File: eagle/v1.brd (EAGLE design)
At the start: 24.2 x 49.6 mm, 48 parts, among them IC2 LT1761, IC4 LT1376-ADJ, Q1 12Mhz, T1 Si2301DS, X1 USB-MICROB

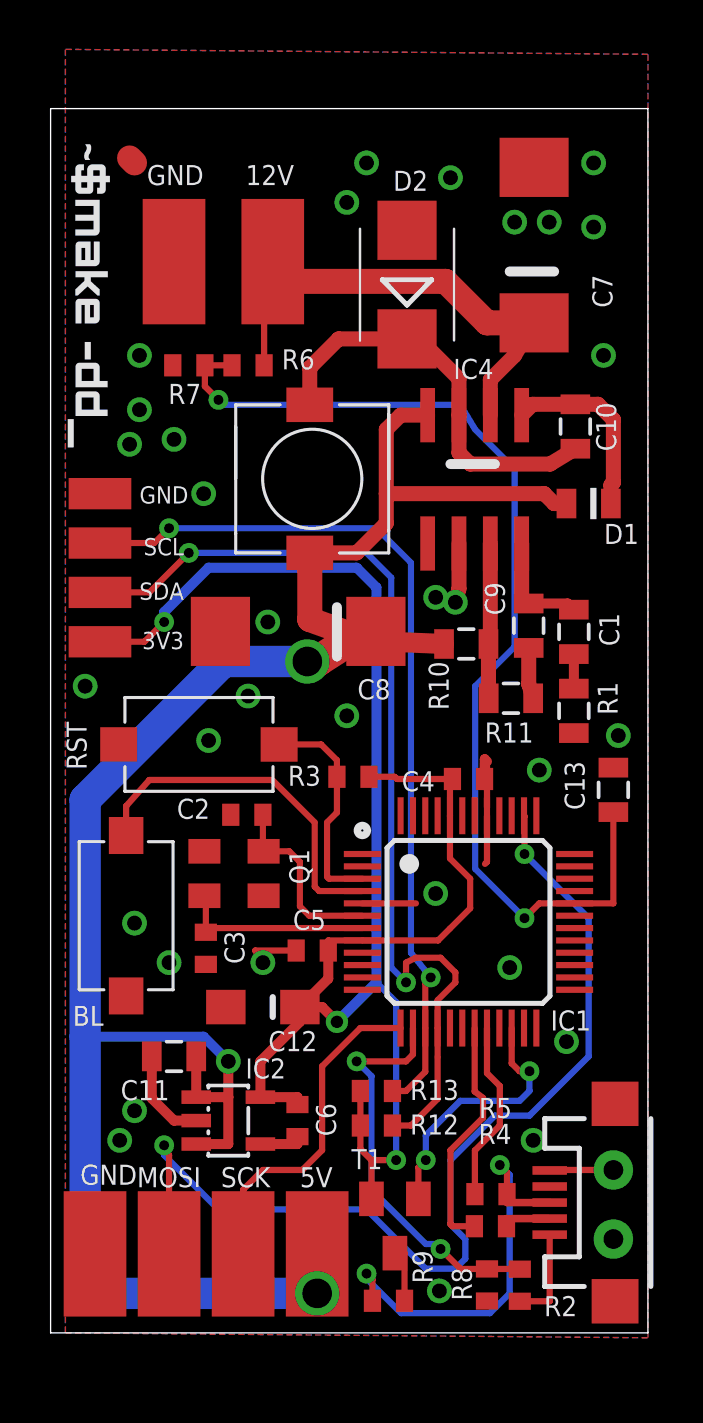
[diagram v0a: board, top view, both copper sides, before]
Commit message: supply circuit via USB for firmware upgrades
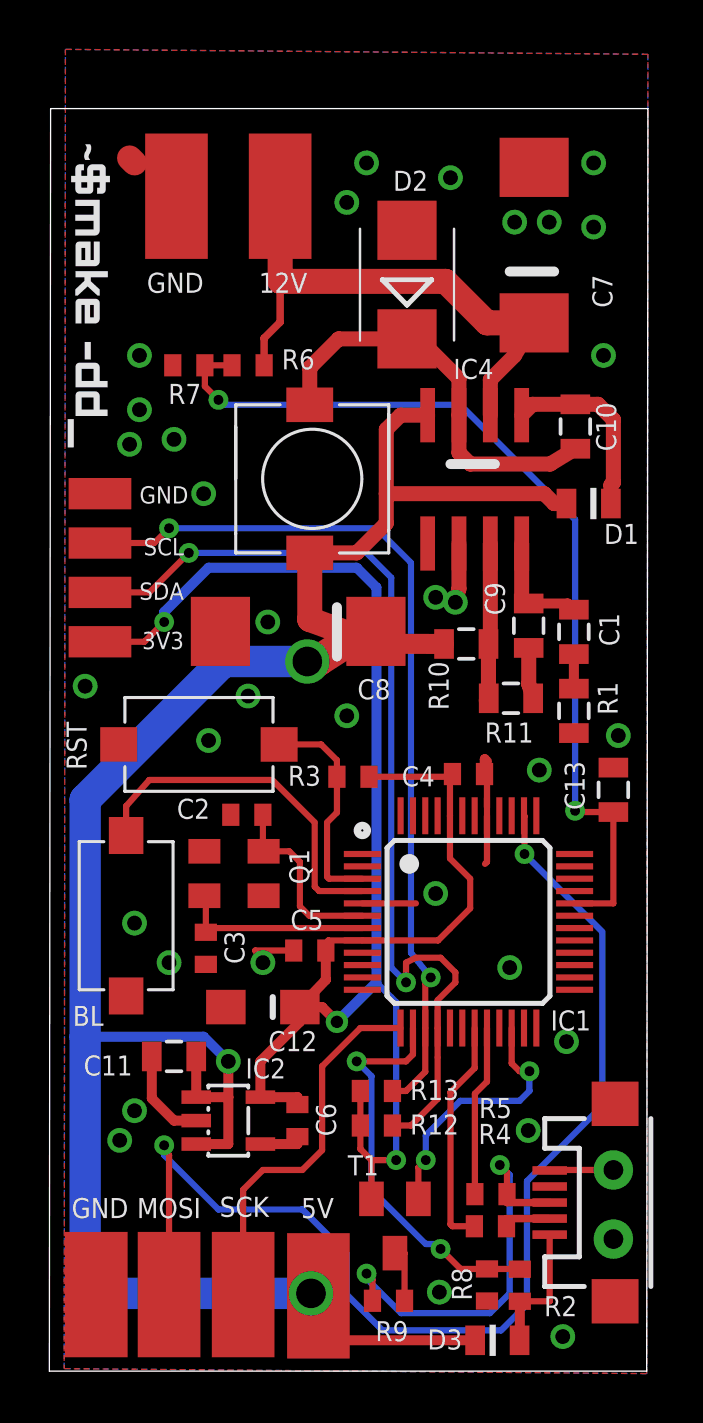
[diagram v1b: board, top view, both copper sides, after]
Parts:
- added D3: 4148, seb:DIODE_0805
- moved 12V 2.67 mm to (11.7, 30.6), turned to 180 degrees
- moved GND 2.65 mm to (7.50, 30.6), turned to 0 degrees
- moved 5V 1.70 mm to (13.2, -13.9)
- moved GND1 1.65 mm to (4.25, -13.8)
- moved MOSI 1.65 mm to (7.20, -13.8)
- moved SCK 1.65 mm to (10.2, -13.8)
- moved C4 0.20 mm to (19.3, 7.24)
- moved C5 0.10 mm to (12.9, 0.09)
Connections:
- net +5V: now also D3.1
- net +5V_USB: now also D3.2
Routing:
- net +5V: track 83.8 -> 90.6 mm
- net N$8: track 41.5 -> 47.9 mm
- net ADC: track 43.3 -> 37.8 mm
- net +12V: track 20.7 -> 22.5 mm
- net N$7: track 13.7 -> 15.3 mm
- net +5V_USB: track 3.91 -> 5.50 mm
- net GND: track 20.4 -> 20.1 mm, vias 34 -> 35
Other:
- board size 24.2 x 49.6 mm -> 24.2 x 51.2 mm
